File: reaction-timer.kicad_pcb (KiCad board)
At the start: 2 copper layers, 48 x 80 mm, 38 parts, among them IC1 4026, IC2 4026, IC3 4026, IC5 NE555P, IC6 NE555P, IC7 NE555P

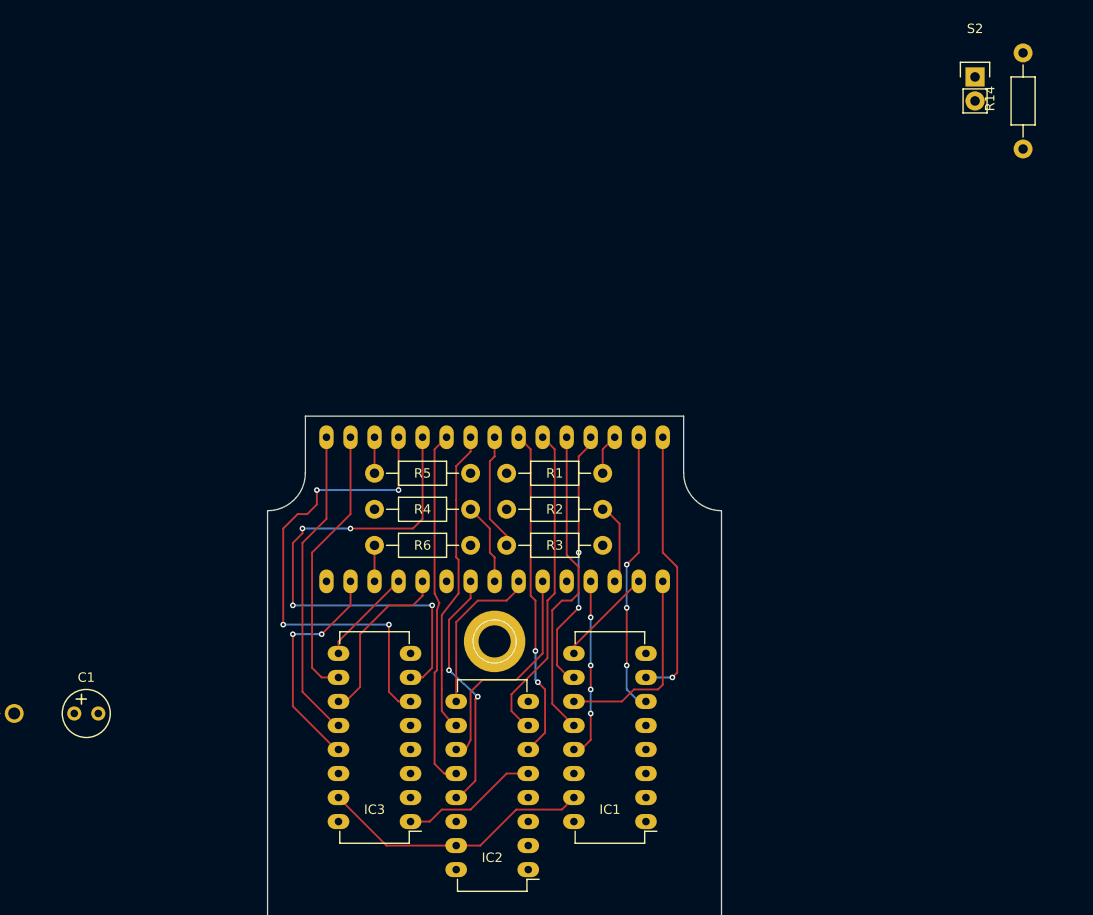
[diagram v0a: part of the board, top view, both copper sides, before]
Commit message: Place and connect S2 and R14
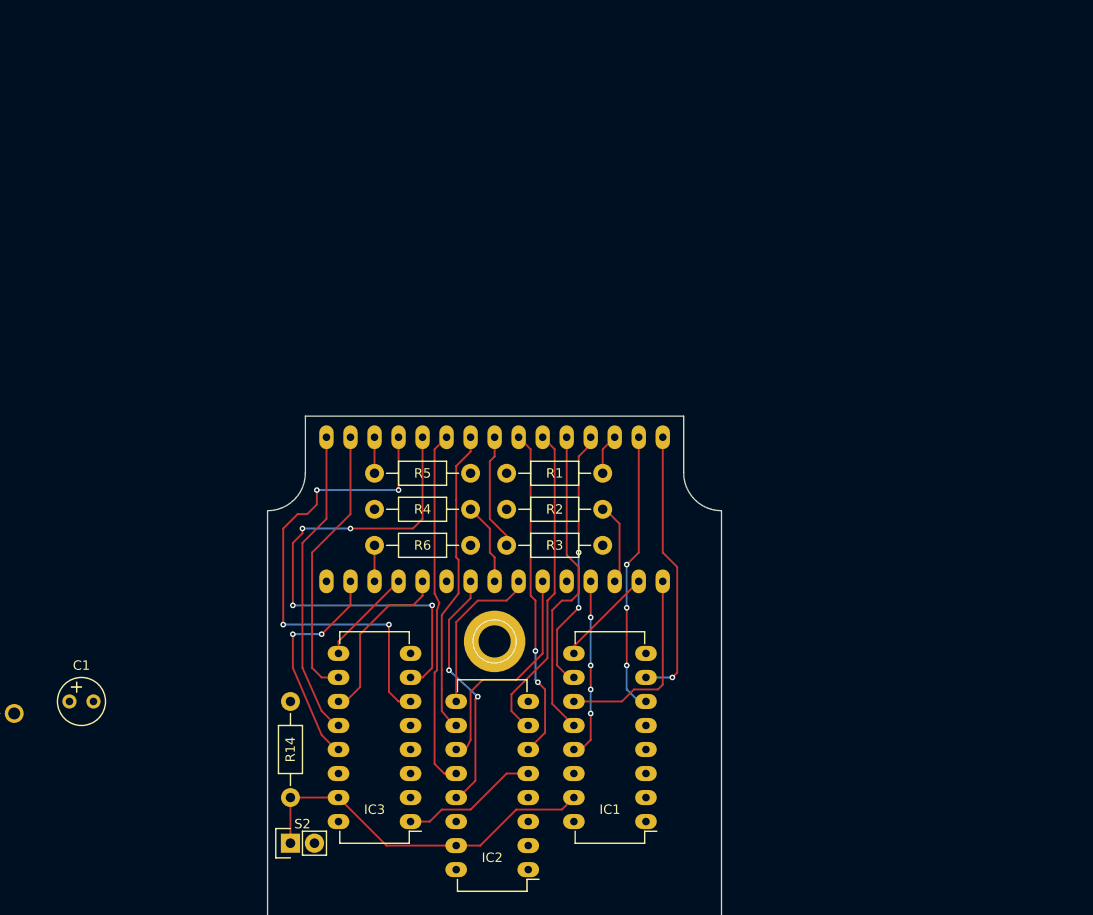
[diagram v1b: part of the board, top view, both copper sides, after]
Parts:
- moved S2 108.7 mm to (59.7, 106.4), turned to 90 degrees
- moved R14 103.5 mm to (59.7, 96.5), turned to 270 degrees
- moved C1 1.37 mm to (36.3, 91.4)
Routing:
- net Net-(IC1-Pad15): track 29.1 -> 39.0 mm
- net /C3: track 24.2 -> 23.6 mm

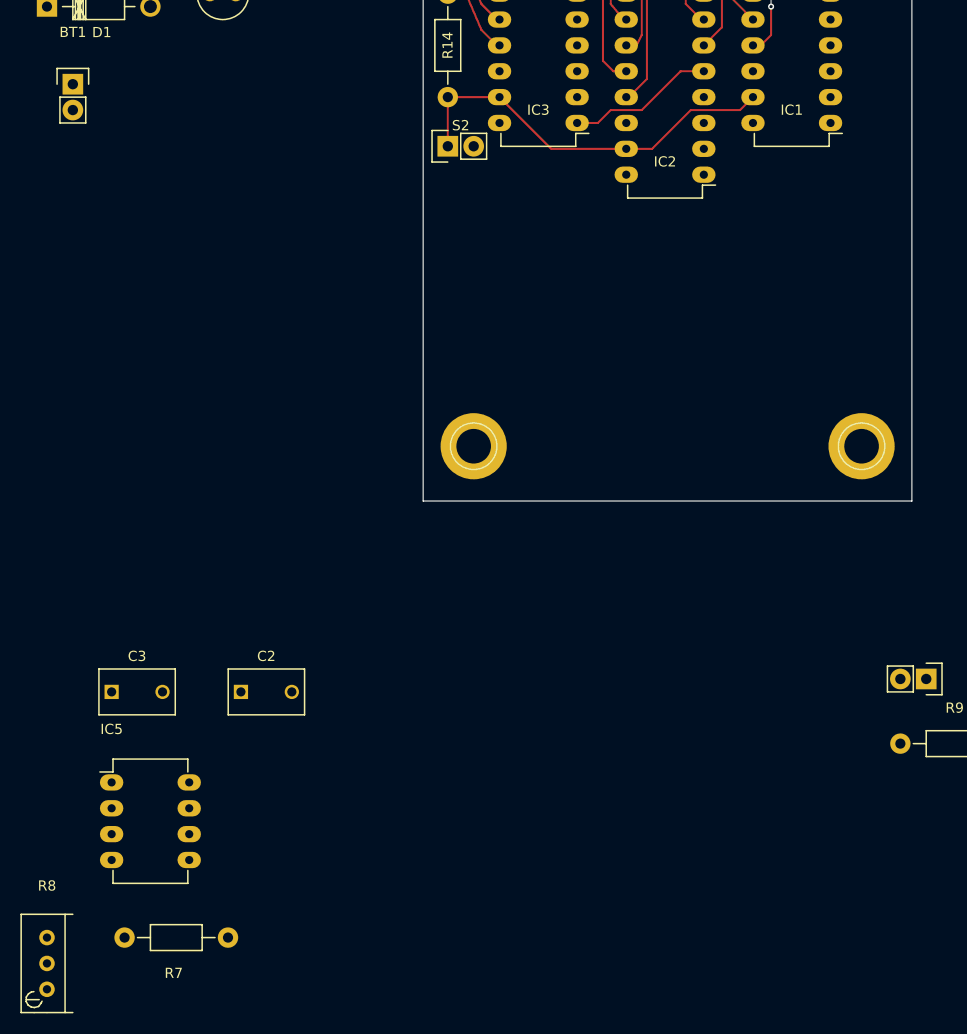
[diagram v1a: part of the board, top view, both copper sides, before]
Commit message: Place and connect IC5
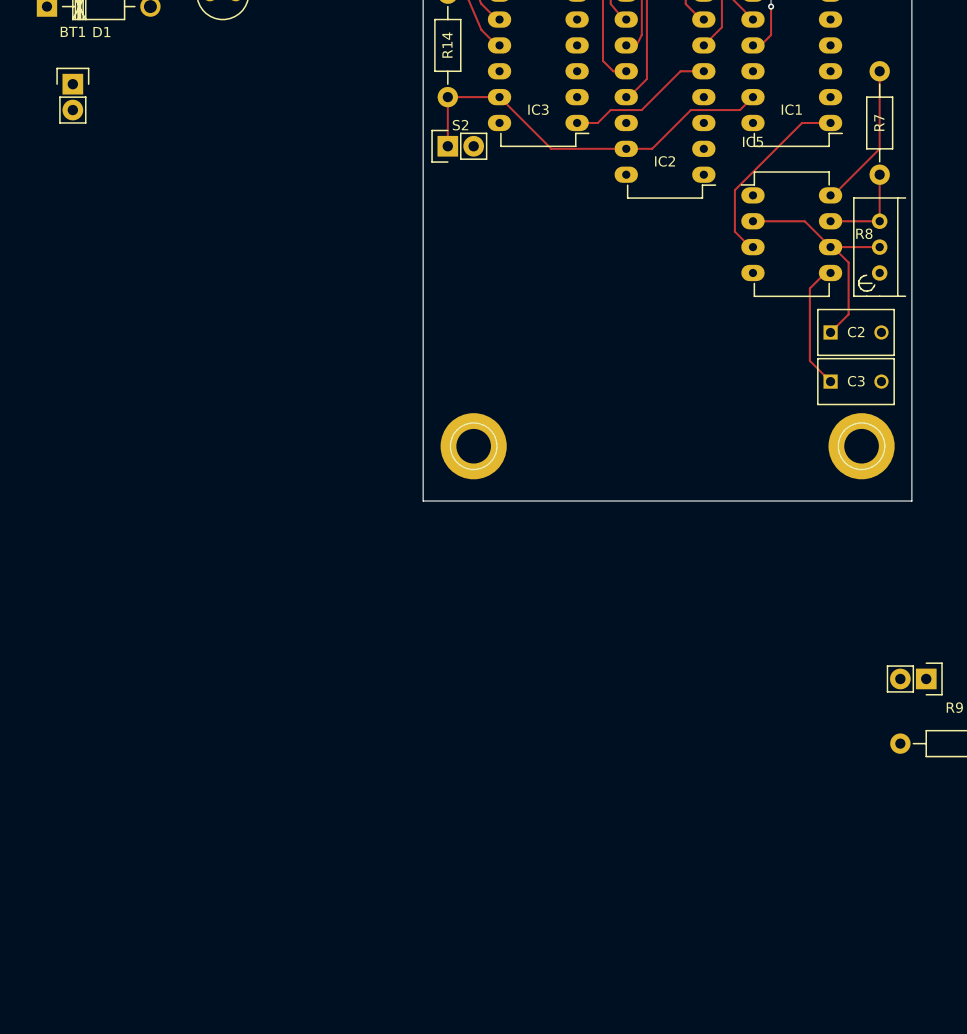
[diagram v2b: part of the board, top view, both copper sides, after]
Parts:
- moved R8 107.9 mm to (102.1, 118.9)
- moved R7 105.7 mm to (102.1, 104.1), turned to 270 degrees
- moved IC5 85.4 mm to (89.7, 111.3)
- moved C3 76.9 mm to (97.3, 129.5)
- moved C2 67.8 mm to (97.3, 124.7)
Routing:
- net Net-(C2-Pad1): track 0.00 -> 23.5 mm
- net Net-(IC1-Pad1): track 0.00 -> 18.6 mm
- net Net-(C1-Pad1): track 0.00 -> 14.3 mm
- net Net-(C3-Pad1): track 0.00 -> 12.6 mm
- net Net-(IC5-Pad7): track 0.00 -> 9.40 mm
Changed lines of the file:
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@@
   (general
     (links 104)
-    (no_connects 72)
+    (no_connects 64)
     (area 17.504999 61.244999 204.617501 195.285)
     (thickness 1.6)
     (drawings 8)
-    (tracks 203)
+    (tracks 224)
     (zones 0)
     (modules 38)
@@
   )
   (module Capacitors_ThroughHole:C_Disc_D7.5_P5 (layer F.Cu)
-    (at 39.37 160.02)
+    (at 97.282 124.714)
     (descr "Capacitor 7.5mm Disc, Pitch 5mm")
     (tags Capacitor)
-    (fp_text reference C2 (at 2.5 -3.5) (layer F.SilkS)
+    (fp_text reference C2 (at 2.54 0) (layer F.SilkS)
       (effects (font (size 1 1) (thickness 0.15)))
     )
@@
   )
   (module Capacitors_ThroughHole:C_Disc_D7.5_P5 (layer F.Cu)
-    (at 26.67 160.02)
+    (at 97.282 129.54)
     (descr "Capacitor 7.5mm Disc, Pitch 5mm")
     (tags Capacitor)
-    (fp_text reference C3 (at 2.5 -3.5) (layer F.SilkS)
+    (fp_text reference C3 (at 2.54 0) (layer F.SilkS)
       (effects (font (size 1 1) (thickness 0.15)))
     )
@@
   )
   (module Housings_DIP:DIP-8_W7.62mm_LongPads (layer F.Cu)
-    (at 26.67 168.91)
+    (at 89.662 111.252)
     (descr "8-lead dip package, row spacing 7.62 mm (300 mils), longer pads")
     (tags "dil dip 2.54 300")
@@
   )
   (module Resistors_ThroughHole:Resistor_Horizontal_RM10mm (layer F.Cu)
-    (at 33.02 184.15 180)
+    (at 102.108 104.14 270)
     (descr "Resistor, Axial,  RM 10mm, 1/3W,")
     (tags "Resistor, Axial, RM 10mm, 1/3W,")
-    (fp_text reference R7 (at 0.24892 -3.50012 180) (layer F.SilkS)
-      (effects (font (size 1 1) (thickness 0.15)))
-    )
-    (fp_text value R (at 3.81 3.81 180) (layer F.Fab)
+    (fp_text reference R7 (at 0 0 270) (layer F.SilkS)
+      (effects (font (size 1 1) (thickness 0.15)))
+    )
+    (fp_text value R (at 3.81 3.81 270) (layer F.Fab)
       (effects (font (size 1 1) (thickness 0.15)))
     )
@@
     (fp_line (start -2.54 0) (end -3.81 0) (layer F.SilkS) (width 0.15))
     (fp_line (start 2.54 0) (end 3.81 0) (layer F.SilkS) (width 0.15))
-    (pad 1 thru_hole circle (at -5.08 0 180) (size 1.99898 1.99898) (drill 1.00076) (layers *.Cu *.SilkS *.Mask)
-      (net 33 "Net-(C1-Pad1)"))
-    (pad 2 thru_hole circle (at 5.08 0 180) (size 1.99898 1.99898) (drill 1.00076) (layers *.Cu *.SilkS *.Mask)
+    (pad 1 thru_hole circle (at -5.08 0 270) (size 1.99898 1.99898) (drill 1.00076) (layers *.Cu *.SilkS *.Mask)
+      (net 33 "Net-(C1-Pad1)"))
+    (pad 2 thru_hole circle (at 5.08 0 270) (size 1.99898 1.99898) (drill 1.00076) (layers *.Cu *.SilkS *.Mask)
       (net 45 "Net-(IC5-Pad7)"))
     (model Resistors_ThroughHole.3dshapes/Resistor_Horizontal_RM10mm.wrl
@@
   )
   (module Potentiometers:Potentiometer_Bourns_3296W_3-8Zoll_Inline_ScrewUp (layer F.Cu)
-    (at 20.32 189.23)
+    (at 102.108 118.872)
     (descr "3296, 3/8, Square, Trimpot, Trimming, Potentiometer, Bourns")
     (tags "3296, 3/8, Square, Trimpot, Trimming, Potentiometer, Bourns")
-    (fp_text reference R8 (at 0 -10.16) (layer F.SilkS)
+    (fp_text reference R8 (at -1.524 -3.81) (layer F.SilkS)
       (effects (font (size 1 1) (thickness 0.15)))
     )
@@
   (segment (start 73.66 88.9) (end 74.676 87.884) (width 0.2) (layer F.Cu) (net 30))
   (segment (start 72.39 88.9) (end 73.66 88.9) (width 0.2) (layer F.Cu) (net 30))
+  (segment (start 97.282 111.252) (end 97.536 111.252) (width 0.2) (layer F.Cu) (net 33) (status C00000))
+  (segment (start 97.536 111.252) (end 102.108 106.68) (width 0.2) (layer F.Cu) (net 33) (status 400000))
+  (segment (start 102.108 106.68) (end 102.108 99.06) (width 0.2) (layer F.Cu) (net 33) (status 800000))
+  (segment (start 97.282 116.332) (end 102.108 116.332) (width 0.2) (layer F.Cu) (net 34) (status C00000))
+  (segment (start 97.282 116.332) (end 97.536 116.332) (width 0.2) (layer F.Cu) (net 34) (status C00000))
+  (segment (start 97.536 116.332) (end 99.06 117.856) (width 0.2) (layer F.Cu) (net 34) (status 400000))
+  (segment (start 99.06 122.936) (end 97.282 124.714) (width 0.2) (layer F.Cu) (net 34) (status 800000))
+  (segment (start 99.06 117.856) (end 99.06 122.936) (width 0.2) (layer F.Cu) (net 34))
+  (segment (start 89.662 113.792) (end 94.742 113.792) (width 0.2) (layer F.Cu) (net 34))
+  (segment (start 94.742 113.792) (end 97.282 116.332) (width 0.2) (layer F.Cu) (net 34))
+  (segment (start 97.282 118.872) (end 96.774 118.872) (width 0.2) (layer F.Cu) (net 35) (status C00000))
+  (segment (start 96.774 118.872) (end 95.25 120.396) (width 0.2) (layer F.Cu) (net 35) (status 400000))
+  (segment (start 95.25 120.396) (end 95.25 127.508) (width 0.2) (layer F.Cu) (net 35))
+  (segment (start 95.25 127.508) (end 97.282 129.54) (width 0.2) (layer F.Cu) (net 35) (status 800000))
+  (segment (start 89.662 116.332) (end 89.408 116.332) (width 0.2) (layer F.Cu) (net 40) (status C00000))
+  (segment (start 89.408 116.332) (end 87.884 114.808) (width 0.2) (layer F.Cu) (net 40) (status 400000))
+  (segment (start 87.884 114.808) (end 87.884 110.744) (width 0.2) (layer F.Cu) (net 40))
+  (segment (start 87.884 110.744) (end 94.488 104.14) (width 0.2) (layer F.Cu) (net 40))
+  (segment (start 94.488 104.14) (end 97.282 104.14) (width 0.2) (layer F.Cu) (net 40) (status 800000))
   (segment (start 69.85 106.68) (end 64.77 101.6) (width 0.2) (layer F.Cu) (net 43))
   (segment (start 77.216 106.68) (end 69.85 106.68) (width 0.2) (layer F.Cu) (net 43))
@@
   (segment (start 82.55 99.06) (end 84.836 99.06) (width 0.2) (layer F.Cu) (net 44))
   (segment (start 72.39 104.14) (end 74.422 104.14) (width 0.2) (layer F.Cu) (net 44))
+  (segment (start 102.108 113.792) (end 102.108 109.22) (width 0.2) (layer F.Cu) (net 45) (status C00000))
+  (segment (start 97.282 113.792) (end 102.108 113.792) (width 0.2) (layer F.Cu) (net 45) (status C00000))
 )

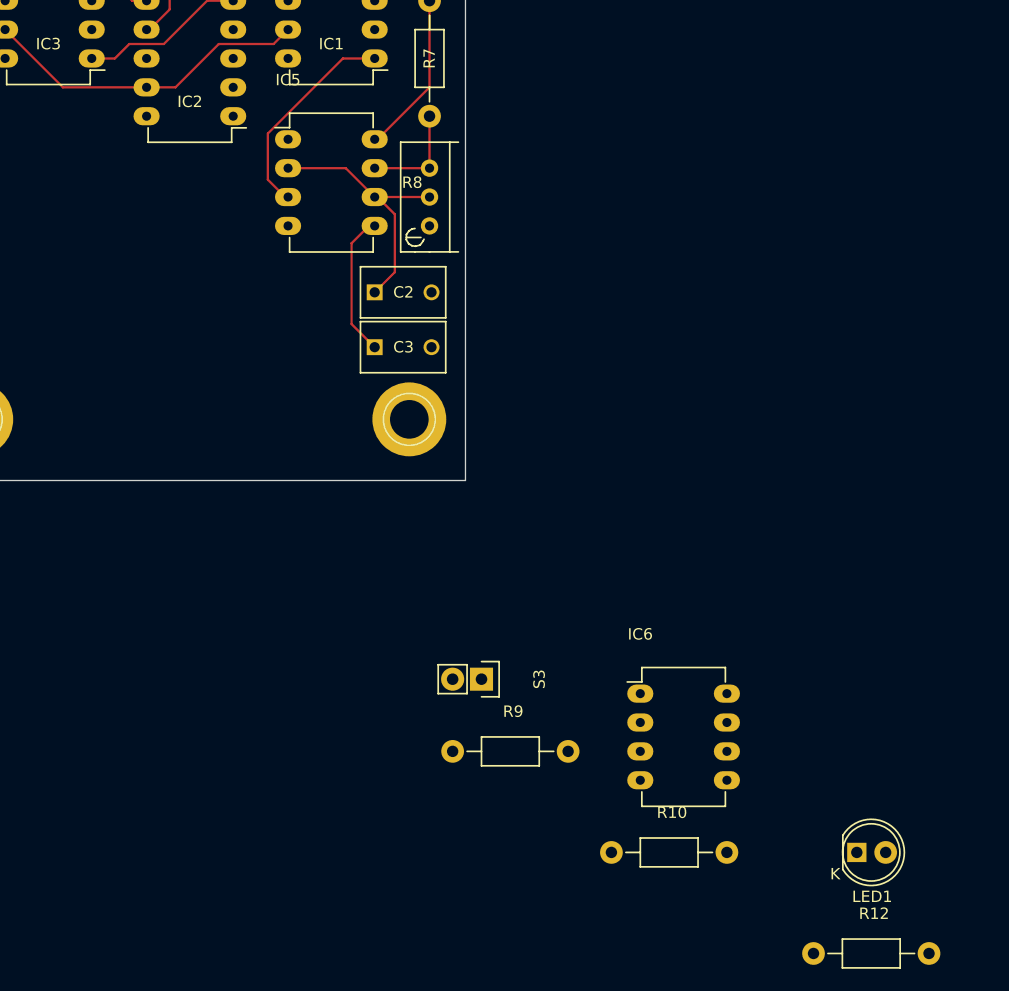
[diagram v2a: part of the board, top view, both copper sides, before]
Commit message: Place and connect IC6
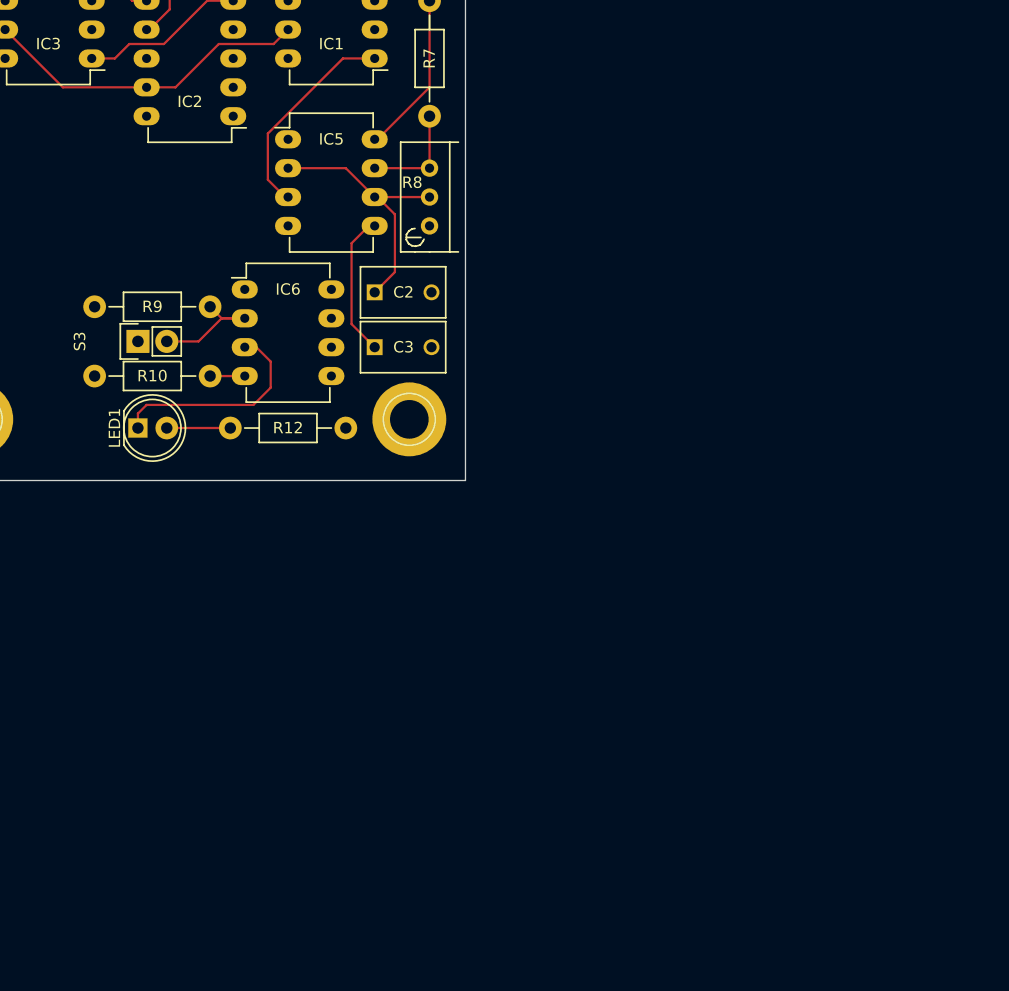
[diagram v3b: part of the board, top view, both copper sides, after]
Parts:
- moved LED1 73.4 mm to (76.5, 136.7)
- moved R12 69.1 mm to (89.7, 136.7), turned to 180 degrees
- moved R10 61.8 mm to (77.7, 132.1), turned to 180 degrees
- moved R9 50.2 mm to (77.7, 126.0), turned to 180 degrees
- moved IC6 49.8 mm to (85.9, 124.5)
- moved S3 42.4 mm to (76.5, 129.0), turned to 90 degrees
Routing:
- net Net-(IC1-Pad2): track 0.00 -> 19.0 mm
- net Net-(IC6-Pad2): track 0.00 -> 11.2 mm
- net Net-(LED1-Pad2): track 0.00 -> 5.59 mm
- net Net-(C4-Pad2): track 0.00 -> 3.05 mm
